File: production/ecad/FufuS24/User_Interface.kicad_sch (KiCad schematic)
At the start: 0 parts

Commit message: added micro usb, LDO regulator, and HDMI
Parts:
- added J3: HDMI_A, symbol Connector:HDMI_A
- added J4: USB_B_Micro, symbol Connector:USB_B_Micro
- added U9: NCP115ASN330T2G, TSOP-5-483-N_ONS, symbol NCP115ASN330:NCP115ASN330T2G
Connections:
- new net +3.3V: U9.5 (OUT)
- new net GND: J4.5 (GND), J4.6 (Shield), U9.2 (GND)
- new net USB_D+: J4.3 (D+)
- new net USB_D-: J4.2 (D-)
- new net VBUS: J4.1 (VBUS), U9.1 (IN), U9.3 (EN)
- no-connect marks 0 -> 1

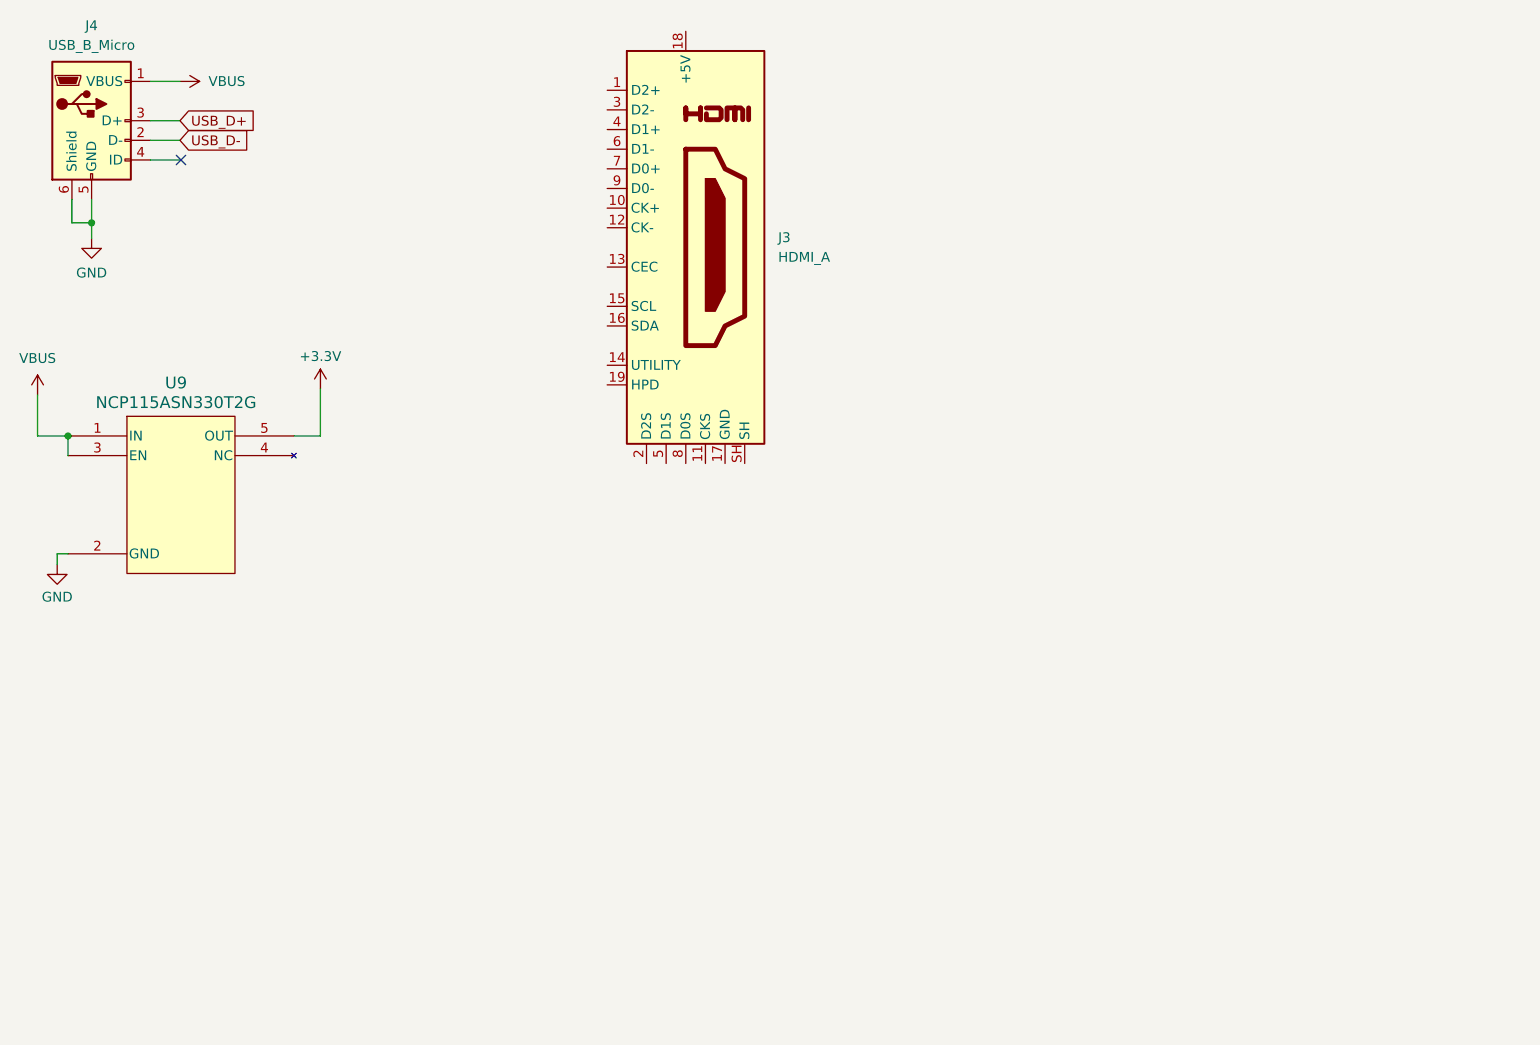
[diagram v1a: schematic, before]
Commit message: Added flags and connections to HDMI
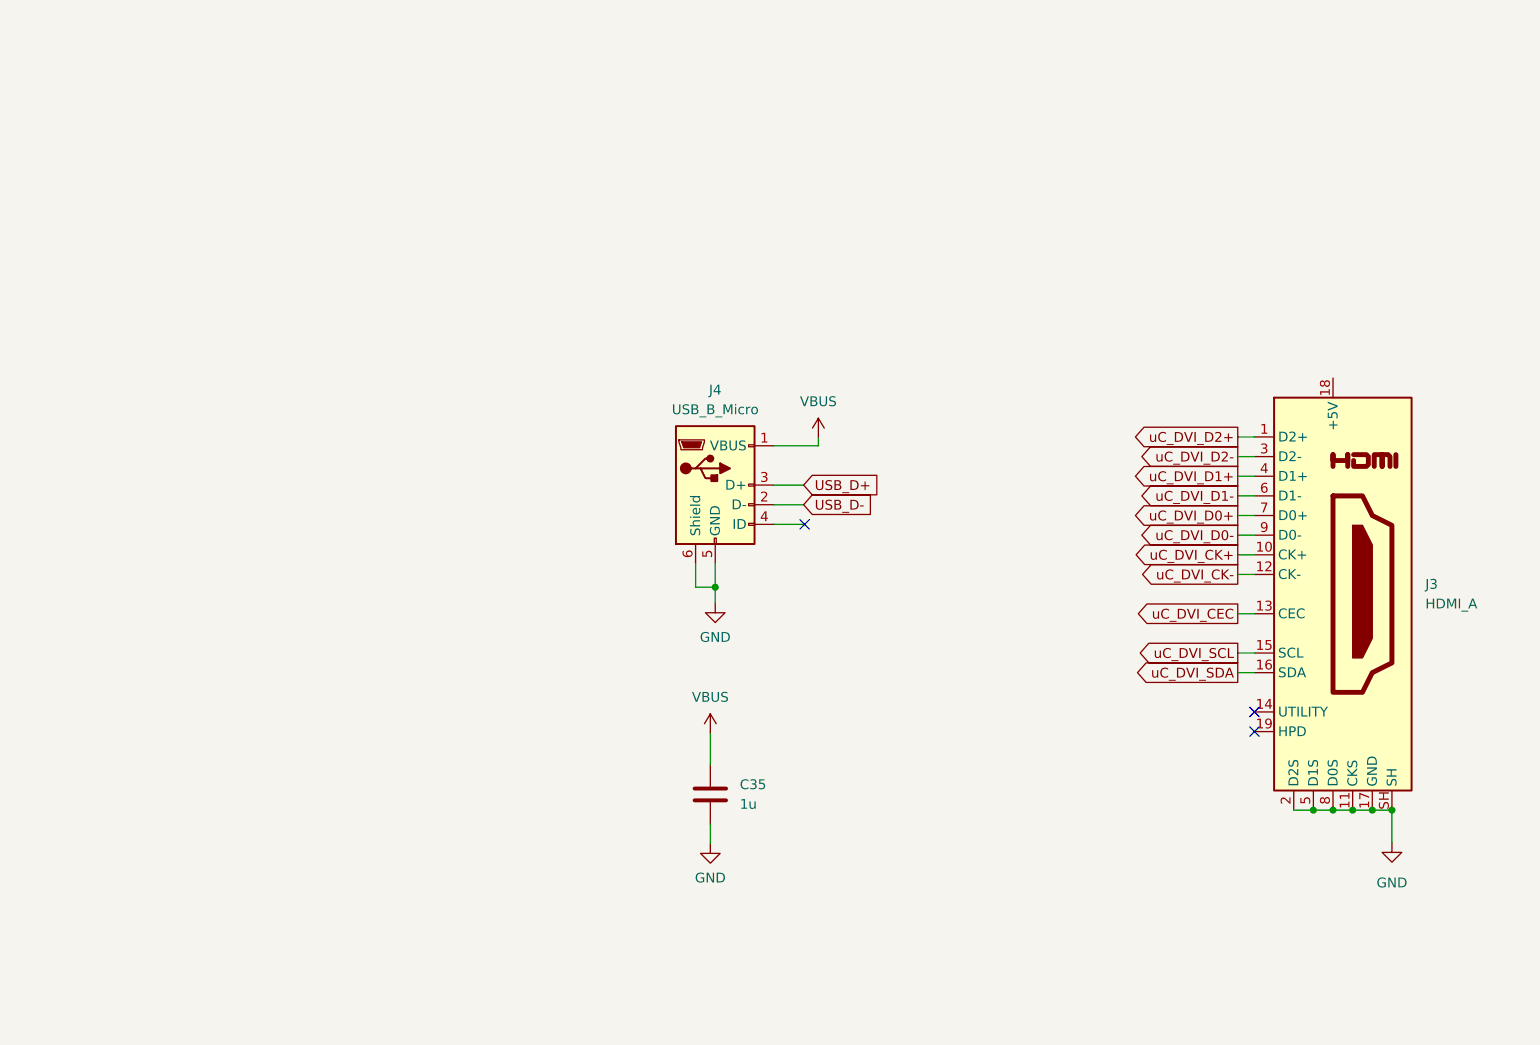
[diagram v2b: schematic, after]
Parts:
- removed U9: NCP115ASN330T2G, TSOP-5-483-N_ONS, symbol NCP115ASN330:NCP115ASN330T2G
- added C35: 1u, symbol Device:C
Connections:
- net GND: now also J3.11 (CKS), J3.17 (GND), J3.2 (D2S), J3.5 (D1S), J3.8 (D0S), J3.SH, C35.2
- net VBUS: now also C35.1
- net uC_DVI_D2+: now reaches J3.1 (D2+)
- net uC_DVI_CK+: now reaches J3.10 (CK+)
- net uC_DVI_CK-: now reaches J3.12 (CK-)
- net uC_DVI_CEC: now reaches J3.13 (CEC)
- net uC_DVI_SCL: now reaches J3.15 (SCL)
- net uC_DVI_SDA: now reaches J3.16 (SDA)
- net uC_DVI_D2-: now reaches J3.3 (D2-)
- net uC_DVI_D1+: now reaches J3.4 (D1+)
- net uC_DVI_D1-: now reaches J3.6 (D1-)
- net uC_DVI_D0+: now reaches J3.7 (D0+)
- net uC_DVI_D0-: now reaches J3.9 (D0-)
- no-connect marks 1 -> 3
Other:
- moved on the sheet: J3, J4

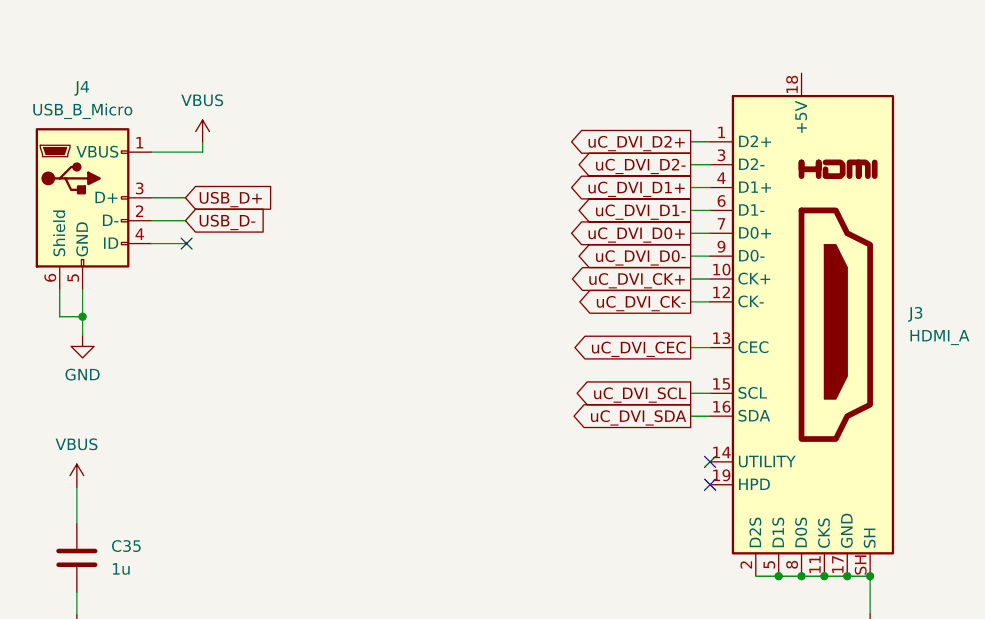
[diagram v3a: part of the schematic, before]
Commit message: Update User_Interface.kicad_sch
Fixed power to mUSB and HDMI
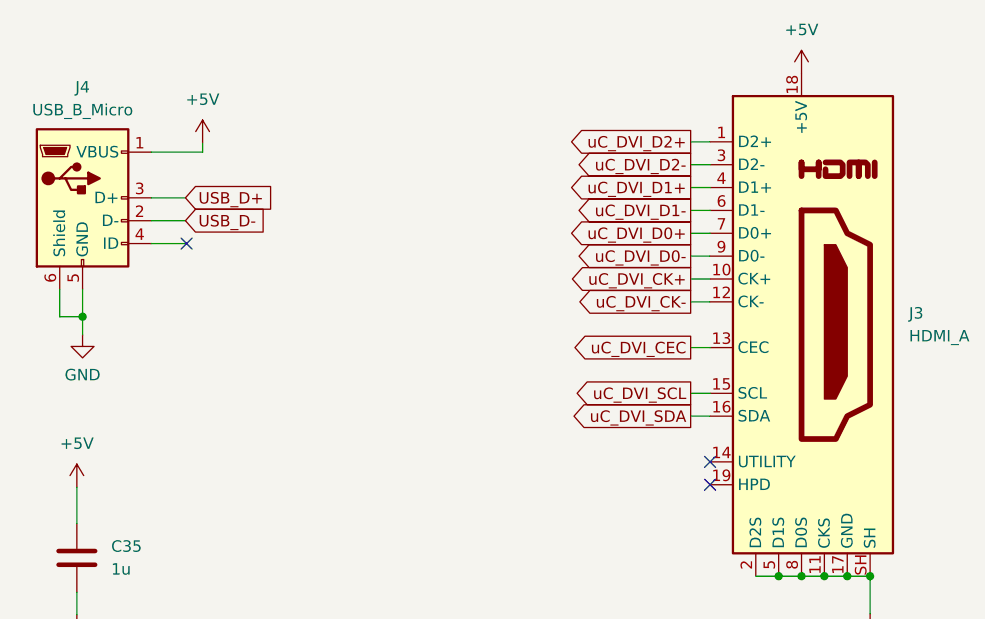
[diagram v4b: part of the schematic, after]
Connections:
- net VBUS is gone; now on net +5V: C35.1, J4.1 (VBUS)
- net +5V: now reaches J3.18 (+5V)
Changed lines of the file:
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@@
+    )
+  )
+  (symbol (lib_id "power:+5V") (at 124.587 73.406 0) (unit 1)
+    (in_bom yes) (on_board yes) (dnp no) (fields_autoplaced)
+    (property "Reference" "#PWR063" (at 124.587 77.216 0)
+      (effects (font (size 1.27 1.27)) hide)
+    )
+    (property "Value" "+5V" (at 124.587 68.58 0)
+      (effects (font (size 1.27 1.27)))
+    )
+    (property "Footprint" "" (at 124.587 73.406 0)
+      (effects (font (size 1.27 1.27)) hide)
+    )
+    (property "Datasheet" "" (at 124.587 73.406 0)
+      (effects (font (size 1.27 1.27)) hide)
+    )
+    (pin "1")
+    (instances
+      (project "FufuS24"
+        (path "/c4c3980b-c8c0-435e-abdc-bbed2349d7ac/876a98ff-842e-4695-a72d-b69ed233d34f"
+          (reference "#PWR063") (unit 1)
+        )
+      )
     )
   )
@@
     )
   )
-  (symbol (lib_id "power:VBUS") (at 110.617 111.633 0) (unit 1)
+  (symbol (lib_id "power:+5V") (at 110.617 111.633 0) (unit 1)
     (in_bom yes) (on_board yes) (dnp no) (fields_autoplaced)
-    (property "Reference" "#PWR068" (at 110.617 115.443 0)
+    (property "Reference" "#PWR066" (at 110.617 115.443 0)
       (effects (font (size 1.27 1.27)) hide)
     )
-    (property "Value" "VBUS" (at 110.617 106.934 0)
+    (property "Value" "+5V" (at 110.617 106.807 0)
       (effects (font (size 1.27 1.27)))
     )
@@
       (project "FufuS24"
         (path "/c4c3980b-c8c0-435e-abdc-bbed2349d7ac/876a98ff-842e-4695-a72d-b69ed233d34f"
-          (reference "#PWR068") (unit 1)
+          (reference "#PWR066") (unit 1)
         )
       )
@@
     )
   )
-  (symbol (lib_id "power:VBUS") (at 124.587 73.406 0) (unit 1)
+  (symbol (lib_id "power:+5V") (at 191.135 65.659 0) (unit 1)
     (in_bom yes) (on_board yes) (dnp no) (fields_autoplaced)
-    (property "Reference" "#PWR063" (at 124.587 77.216 0)
+    (property "Reference" "#PWR067" (at 191.135 69.469 0)
       (effects (font (size 1.27 1.27)) hide)
     )
-    (property "Value" "VBUS" (at 124.587 68.707 0)
+    (property "Value" "+5V" (at 191.135 60.833 0)
       (effects (font (size 1.27 1.27)))
     )
-    (property "Footprint" "" (at 124.587 73.406 0)
+    (property "Footprint" "" (at 191.135 65.659 0)
       (effects (font (size 1.27 1.27)) hide)
     )
-    (property "Datasheet" "" (at 124.587 73.406 0)
+    (property "Datasheet" "" (at 191.135 65.659 0)
       (effects (font (size 1.27 1.27)) hide)
     )
@@
       (project "FufuS24"
         (path "/c4c3980b-c8c0-435e-abdc-bbed2349d7ac/876a98ff-842e-4695-a72d-b69ed233d34f"
-          (reference "#PWR063") (unit 1)
+          (reference "#PWR067") (unit 1)
         )
       )

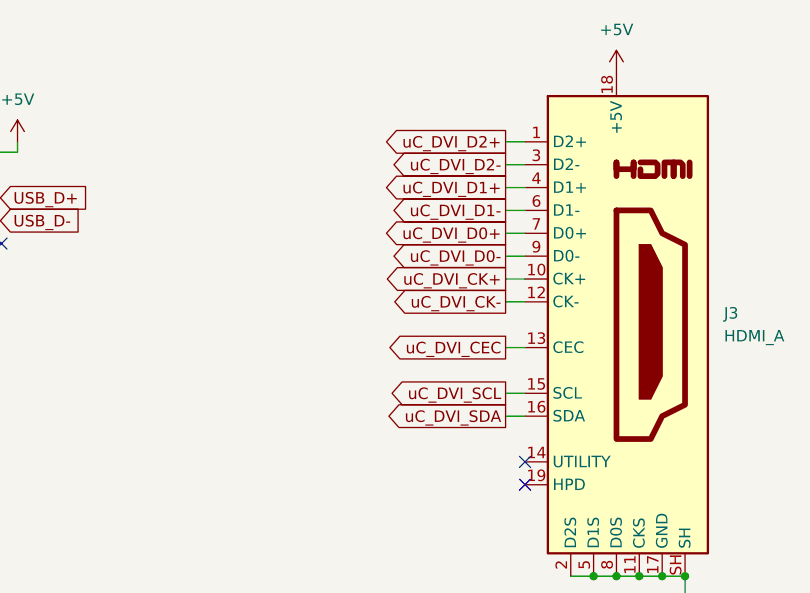
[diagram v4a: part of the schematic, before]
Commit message: Updated Ctrl and UI schems
Added labels to Control and changed nets to output. Updated GPIO pins on UI to reflect what was available.
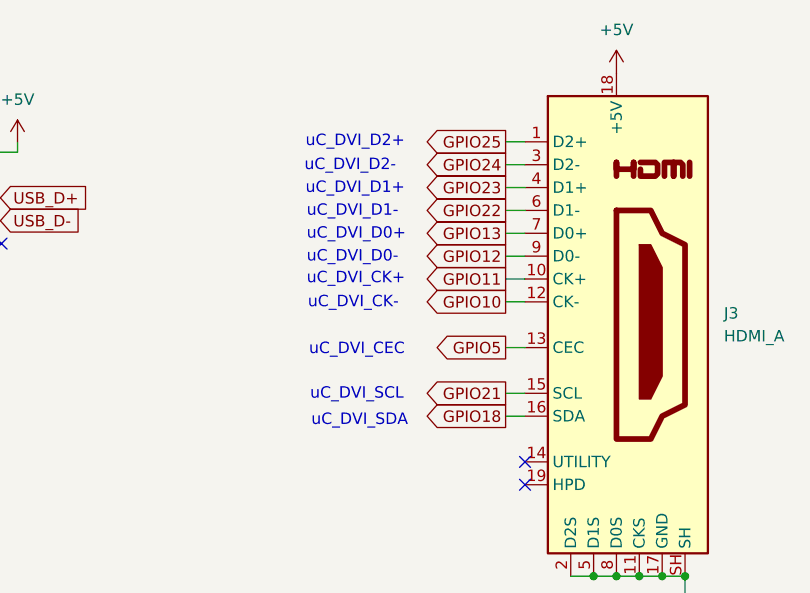
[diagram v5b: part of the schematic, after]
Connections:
- net uC_DVI_CEC renamed GPIO5
- net uC_DVI_CK+ renamed GPIO11
- net uC_DVI_CK- renamed GPIO10
- net uC_DVI_D0+ renamed GPIO13
- net uC_DVI_D0- renamed GPIO12
- net uC_DVI_D1+ renamed GPIO23
- net uC_DVI_D1- renamed GPIO22
- net uC_DVI_D2+ renamed GPIO25
- net uC_DVI_D2- renamed GPIO24
- net uC_DVI_SCL renamed GPIO21
- net uC_DVI_SDA renamed GPIO18
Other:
- note added: "uC_DVI_CEC"
- note added: "uC_DVI_CK+"
- note added: "uC_DVI_CK-"
- note added: "uC_DVI_D0+"
- note added: "uC_DVI_D0-"
- note added: "uC_DVI_D1+"
- note added: "uC_DVI_D1-"
- note added: "uC_DVI_D2+"
- note added: "uC_DVI_D2-"
- note added: "uC_DVI_SCL"
- note added: "uC_DVI_SDA"
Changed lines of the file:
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@@
     (stroke (width 0) (type default))
   )
-  (global_label "uC_DVI_D0+" (shape output) (at 178.816 83.439 180) (fields_autoplaced)
+  (text "uC_DVI_D1-" (at 156.718 81.788 0)
+    (effects (font (size 1.27 1.27)) (justify left bottom))
+  )
+  (text "uC_DVI_SDA" (at 157.226 105.029 0)
+    (effects (font (size 1.27 1.27)) (justify left bottom))
+  )
+  (text "uC_DVI_CEC" (at 156.972 97.155 0)
+    (effects (font (size 1.27 1.27)) (justify left bottom))
+  )
+  (text "uC_DVI_D1+" (at 156.591 79.248 0)
+    (effects (font (size 1.27 1.27)) (justify left bottom))
+  )
+  (text "uC_DVI_SCL" (at 157.099 102.108 0)
+    (effects (font (size 1.27 1.27)) (justify left bottom))
+  )
+  (text "uC_DVI_D0-" (at 156.718 86.868 0)
+    (effects (font (size 1.27 1.27)) (justify left bottom))
+  )
+  (text "uC_DVI_D0+" (at 156.718 84.328 0)
+    (effects (font (size 1.27 1.27)) (justify left bottom))
+  )
+  (text "uC_DVI_CK-" (at 156.845 91.948 0)
+    (effects (font (size 1.27 1.27)) (justify left bottom))
+  )
+  (text "uC_DVI_CK+" (at 156.718 89.281 0)
+    (effects (font (size 1.27 1.27)) (justify left bottom))
+  )
+  (text "uC_DVI_D2-" (at 156.464 76.708 0)
+    (effects (font (size 1.27 1.27)) (justify left bottom))
+  )
+  (text "uC_DVI_D2+" (at 156.591 74.041 0)
+    (effects (font (size 1.27 1.27)) (justify left bottom))
+  )
+  (global_label "GPIO13" (shape output) (at 178.816 83.439 180) (fields_autoplaced)
     (effects (font (size 1.27 1.27)) (justify right))
-    (property "Intersheetrefs" "${INTERSHEET_REFS}" (at 164.4613 83.439 0)
+    (property "Intersheetrefs" "${INTERSHEET_REFS}" (at 168.9365 83.439 0)
       (effects (font (size 1.27 1.27)) (justify right) hide)
     )
   )
-  (global_label "uC_DVI_D2+" (shape output) (at 178.816 73.279 180) (fields_autoplaced)
+  (global_label "GPIO25" (shape output) (at 178.816 73.279 180) (fields_autoplaced)
     (effects (font (size 1.27 1.27)) (justify right))
-    (property "Intersheetrefs" "${INTERSHEET_REFS}" (at 164.4613 73.279 0)
+    (property "Intersheetrefs" "${INTERSHEET_REFS}" (at 168.9365 73.279 0)
       (effects (font (size 1.27 1.27)) (justify right) hide)
     )
@@
     )
   )
-  (global_label "uC_DVI_SDA" (shape output) (at 178.816 103.759 180) (fields_autoplaced)
+  (global_label "GPIO18" (shape output) (at 178.816 103.759 180) (fields_autoplaced)
     (effects (font (size 1.27 1.27)) (justify right))
-    (property "Intersheetrefs" "${INTERSHEET_REFS}" (at 164.9451 103.759 0)
+    (property "Intersheetrefs" "${INTERSHEET_REFS}" (at 168.9365 103.759 0)
       (effects (font (size 1.27 1.27)) (justify right) hide)
     )
   )
-  (global_label "uC_DVI_CEC" (shape output) (at 178.816 96.139 180) (fields_autoplaced)
+  (global_label "GPIO5" (shape output) (at 178.816 96.139 180) (fields_autoplaced)
     (effects (font (size 1.27 1.27)) (justify right))
-    (property "Intersheetrefs" "${INTERSHEET_REFS}" (at 164.8242 96.139 0)
+    (property "Intersheetrefs" "${INTERSHEET_REFS}" (at 170.146 96.139 0)
       (effects (font (size 1.27 1.27)) (justify right) hide)
     )
   )
-  (global_label "uC_DVI_D1-" (shape output) (at 178.816 80.899 180) (fields_autoplaced)
+  (global_label "GPIO22" (shape output) (at 178.816 80.899 180) (fields_autoplaced)
     (effects (font (size 1.27 1.27)) (justify right))
-    (property "Intersheetrefs" "${INTERSHEET_REFS}" (at 164.4613 80.899 0)
+    (property "Intersheetrefs" "${INTERSHEET_REFS}" (at 168.9365 80.899 0)
       (effects (font (size 1.27 1.27)) (justify right) hide)
     )
   )
-  (global_label "uC_DVI_SCL" (shape output) (at 178.816 101.219 180) (fields_autoplaced)
+  (global_label "GPIO21" (shape output) (at 178.816 101.219 180) (fields_autoplaced)
     (effects (font (size 1.27 1.27)) (justify right))
-    (property "Intersheetrefs" "${INTERSHEET_REFS}" (at 165.0056 101.219 0)
+    (property "Intersheetrefs" "${INTERSHEET_REFS}" (at 168.9365 101.219 0)
       (effects (font (size 1.27 1.27)) (justify right) hide)
     )
   )
-  (global_label "uC_DVI_D0-" (shape output) (at 178.816 85.979 180) (fields_autoplaced)
+  (global_label "GPIO12" (shape output) (at 178.816 85.979 180) (fields_autoplaced)
     (effects (font (size 1.27 1.27)) (justify right))
-    (property "Intersheetrefs" "${INTERSHEET_REFS}" (at 164.4613 85.979 0)
+    (property "Intersheetrefs" "${INTERSHEET_REFS}" (at 168.9365 85.979 0)
       (effects (font (size 1.27 1.27)) (justify right) hide)
     )
   )
-  (global_label "uC_DVI_D1+" (shape output) (at 178.816 78.359 180) (fields_autoplaced)
+  (global_label "GPIO23" (shape output) (at 178.816 78.359 180) (fields_autoplaced)
     (effects (font (size 1.27 1.27)) (justify right))
-    (property "Intersheetrefs" "${INTERSHEET_REFS}" (at 164.4613 78.359 0)
+    (property "Intersheetrefs" "${INTERSHEET_REFS}" (at 168.9365 78.359 0)
       (effects (font (size 1.27 1.27)) (justify right) hide)
     )
@@
     )
   )
-  (global_label "uC_DVI_D2-" (shape output) (at 178.816 75.819 180) (fields_autoplaced)
+  (global_label "GPIO24" (shape output) (at 178.816 75.819 180) (fields_autoplaced)
     (effects (font (size 1.27 1.27)) (justify right))
-    (property "Intersheetrefs" "${INTERSHEET_REFS}" (at 164.4613 75.819 0)
+    (property "Intersheetrefs" "${INTERSHEET_REFS}" (at 168.9365 75.819 0)
       (effects (font (size 1.27 1.27)) (justify right) hide)
     )
   )
-  (global_label "uC_DVI_CK+" (shape output) (at 178.816 88.519 180) (fields_autoplaced)
+  (global_label "GPIO11" (shape output) (at 178.816 88.519 180) (fields_autoplaced)
     (effects (font (size 1.27 1.27)) (justify right))
-    (property "Intersheetrefs" "${INTERSHEET_REFS}" (at 164.4008 88.519 0)
+    (property "Intersheetrefs" "${INTERSHEET_REFS}" (at 168.9365 88.519 0)
       (effects (font (size 1.27 1.27)) (justify right) hide)
     )
   )
-  (global_label "uC_DVI_CK-" (shape output) (at 178.816 91.059 180) (fields_autoplaced)
+  (global_label "GPIO10" (shape output) (at 178.816 91.059 180) (fields_autoplaced)
     (effects (font (size 1.27 1.27)) (justify right))
-    (property "Intersheetrefs" "${INTERSHEET_REFS}" (at 164.4008 91.059 0)
+    (property "Intersheetrefs" "${INTERSHEET_REFS}" (at 168.9365 91.059 0)
       (effects (font (size 1.27 1.27)) (justify right) hide)
     )
